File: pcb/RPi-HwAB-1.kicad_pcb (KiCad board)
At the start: 6 copper layers, 65 x 56 mm, 136 parts, among them J1 GPIO, J2 Hirose_FH12-16S, J3 TC2030, M1V1 TestPoint, M1V2 TestPoint, U1 CAT24C256, U10 INA230AIRGTT, U11 MCP9804_DFN, U12 TPSM82903, U13 TPSM82903, U14 AP3441SHE-7B, U2 TPSM82903, U3 LM3880, U4 TXS0102YZP, U5 XC7A100T-FGG484, U6 MT41K256M16LY, U7 TCR2EE135, U8 MX25L3233FZN, U9 INA230AIRGTT, Y1 SiT9365AI-2B2-33E200.000000

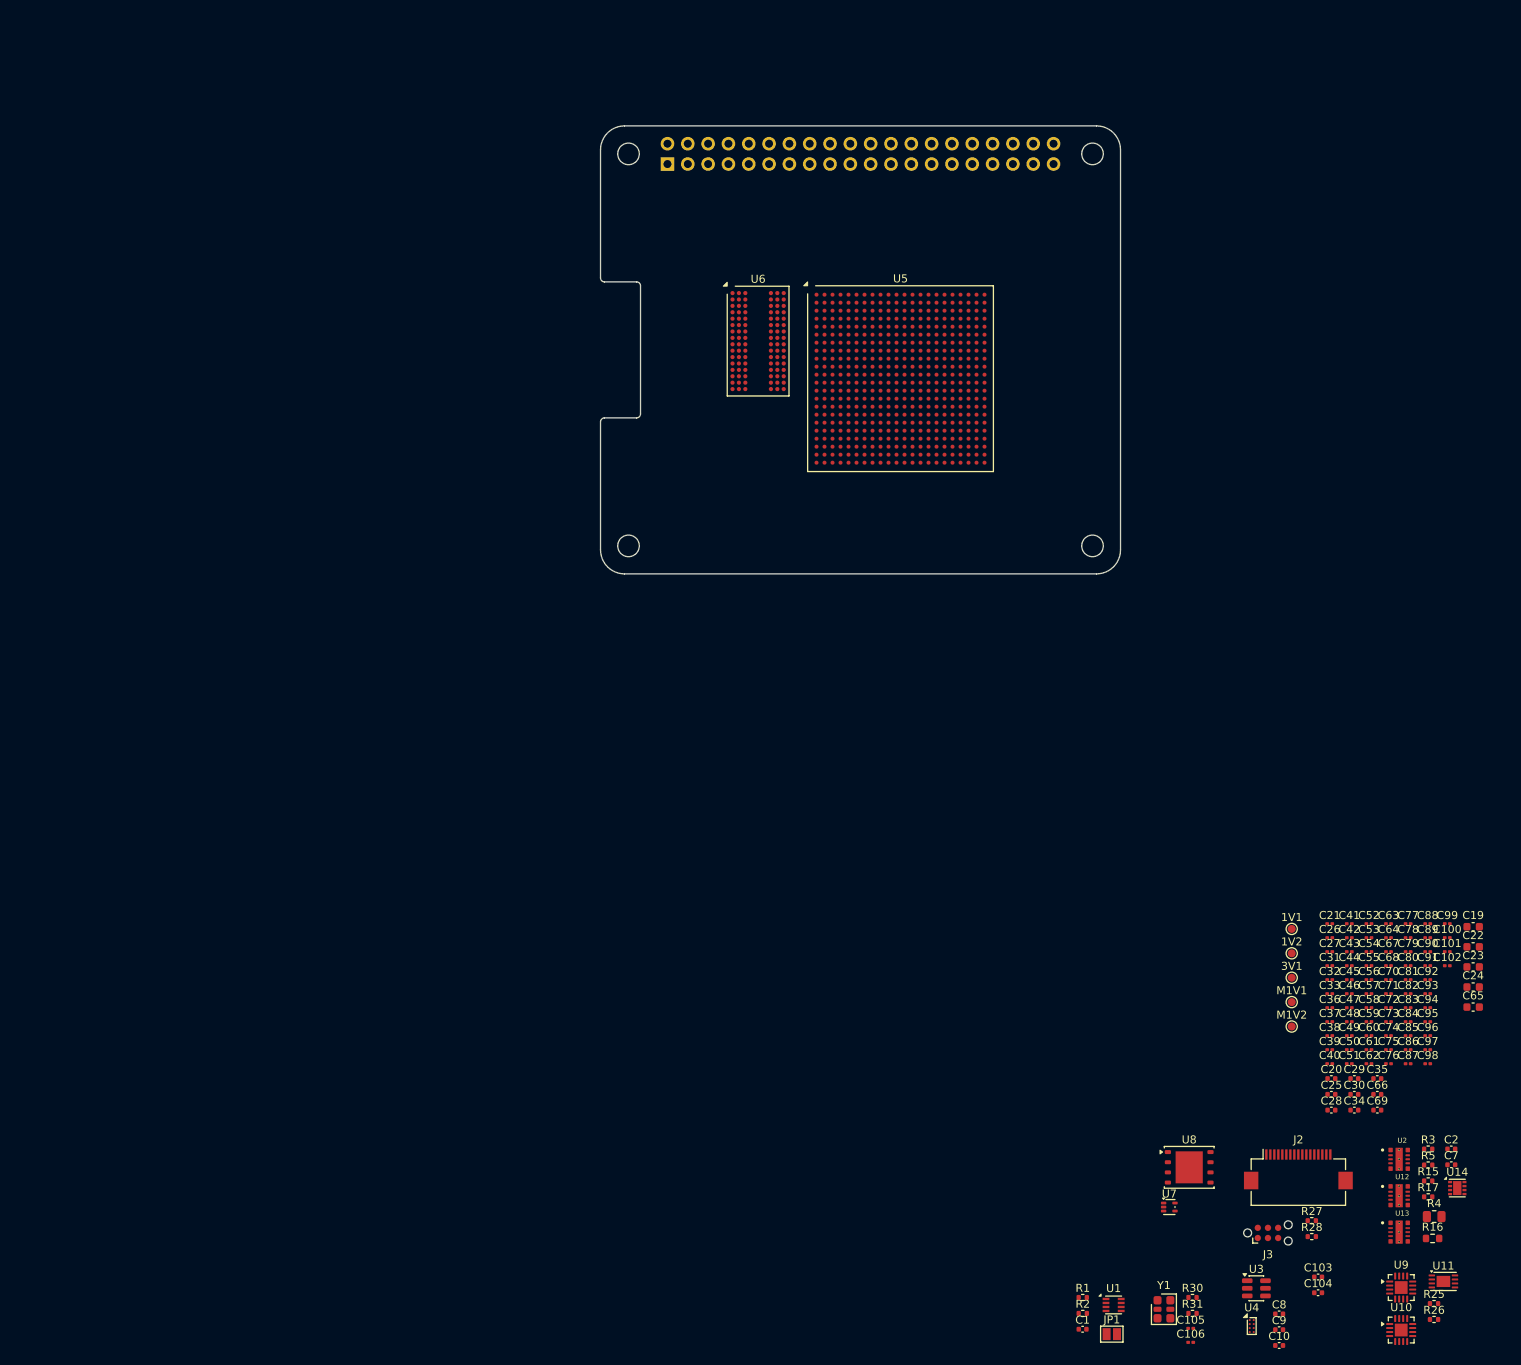
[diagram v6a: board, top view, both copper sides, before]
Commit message: changes to power tree
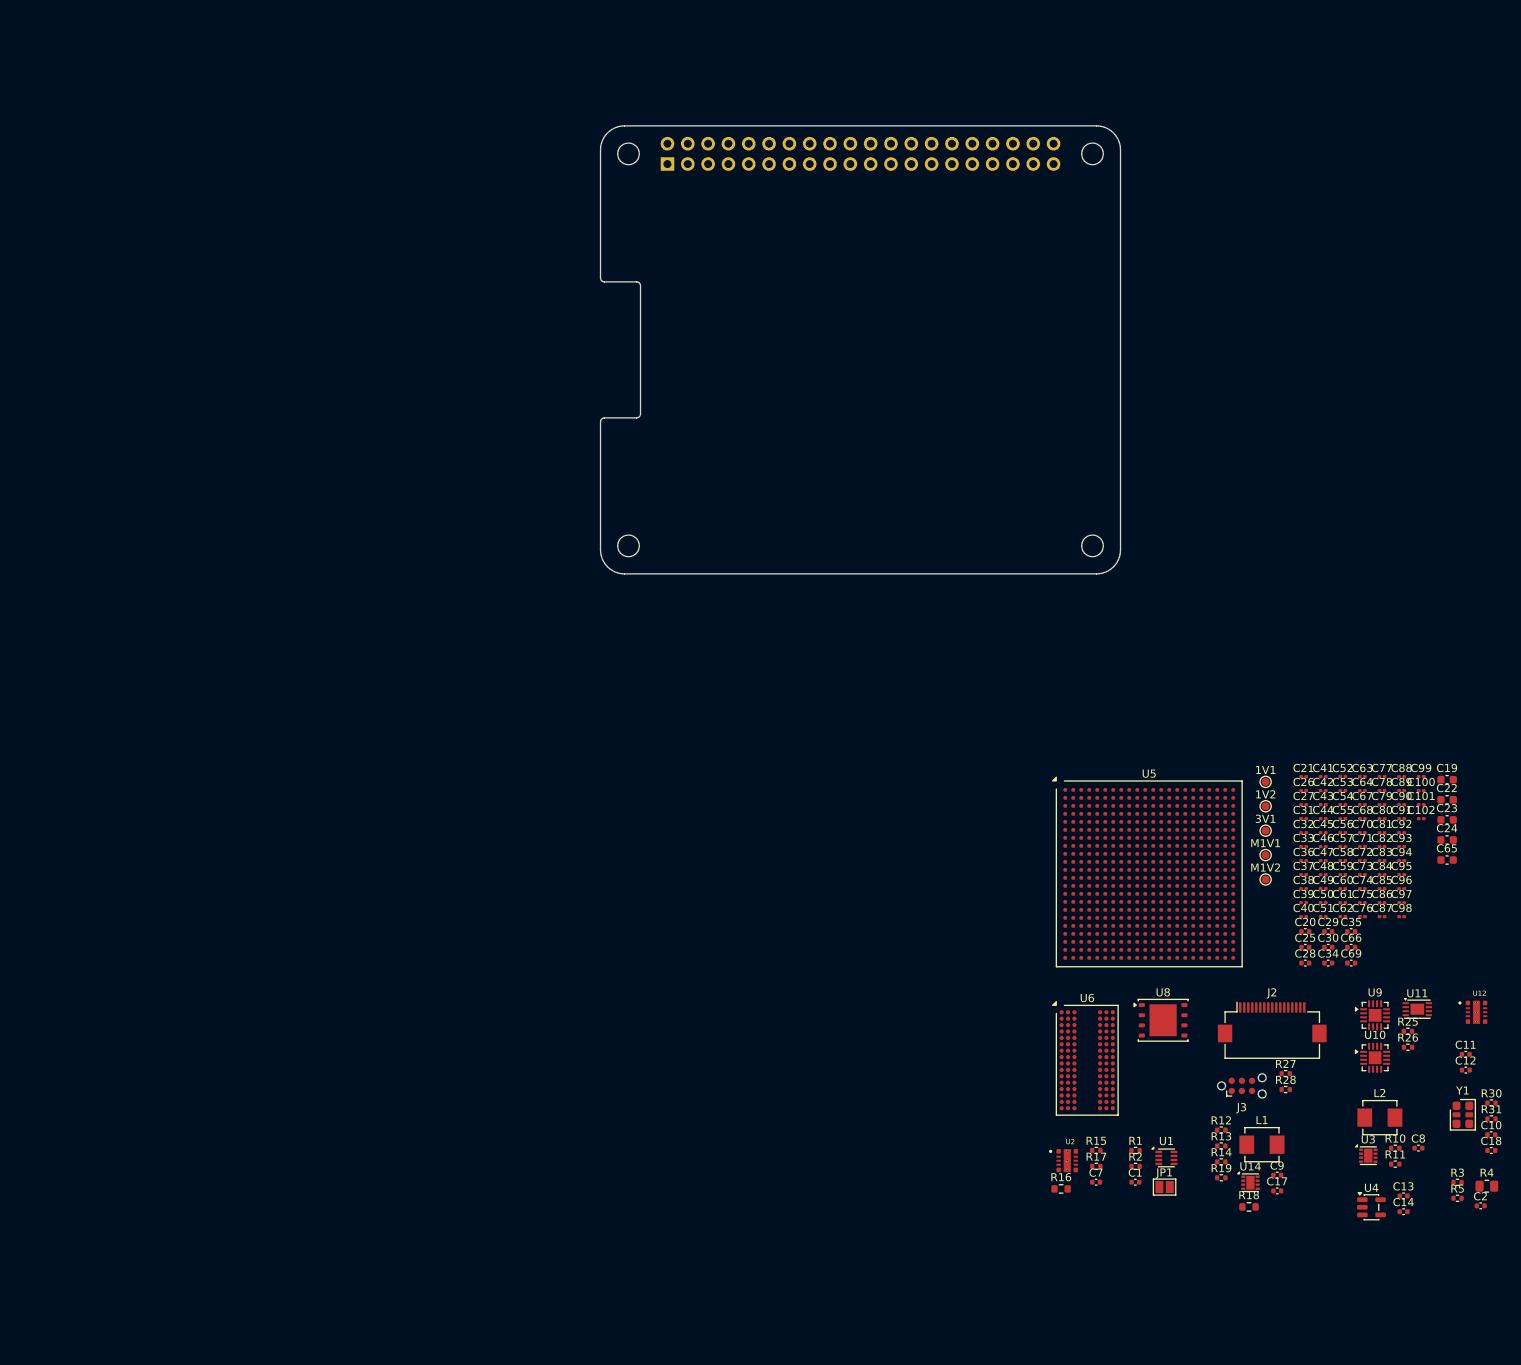
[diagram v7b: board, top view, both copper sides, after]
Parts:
- removed C103, C104: 0.1uF, Capacitor_SMD:C_0402_1005Metric
- removed C105, C106: 0.1uF, Capacitor_SMD:C_0201_0603Metric
- removed U13: TPSM82903, library:TPSM82903SISR
- removed U7: TCR2EE135, Package_TO_SOT_SMD:SOT-553
- added C11: 0.1uF, Capacitor_SMD:C_0402_1005Metric, F.Cu at (208.2, 160.1)
- added C12: 0.1uF, Capacitor_SMD:C_0402_1005Metric, F.Cu at (208.2, 162.0)
- added C13: 1uF, Capacitor_SMD:C_0402_1005Metric, F.Cu at (200.4, 177.8)
- added C14: 1uF, Capacitor_SMD:C_0402_1005Metric, F.Cu at (200.4, 179.7)
- added C17: 0.1uF, Capacitor_SMD:C_0402_1005Metric, F.Cu at (184.6, 177.1)
- added C18: 0.1uF, Capacitor_SMD:C_0402_1005Metric, F.Cu at (211.3, 172.1)
- added L1: 2.2uH, Inductor_SMD:L_Vishay_IHLP-1616, F.Cu at (182.7, 171.3)
- added L2: 2.2uH, Inductor_SMD:L_Vishay_IHLP-1616, F.Cu at (197.4, 168.0)
- added R10: ? 1%, Resistor_SMD:R_0402_1005Metric, F.Cu at (199.3, 171.8)
- added R11: ? 1%, Resistor_SMD:R_0402_1005Metric, F.Cu at (199.3, 173.8)
- added R12: ? 1%, Resistor_SMD:R_0402_1005Metric, F.Cu at (177.6, 169.5)
- added R13: ? 1%, Resistor_SMD:R_0402_1005Metric, F.Cu at (177.6, 171.5)
- added R14: 100, Resistor_SMD:R_0402_1005Metric, F.Cu at (177.6, 173.5)
- added R18: 0.005, Resistor_SMD:R_0603_1608Metric, F.Cu at (181.1, 179.1)
- added R19: 100, Resistor_SMD:R_0402_1005Metric, F.Cu at (177.6, 175.5)
- C8, C9: value 0.1uF -> 4.7nF
- U3: value LM3880 -> AP3441SHE-7B; footprint Package_TO_SOT_SMD:SOT-23-6 -> Package_DFN_QFN:DFN-8-1EP_2x2mm_P0.5mm_EP1.05x1.75mm
- U4: value TXS0102YZP -> TLV74312PDBVR; footprint Package_BGA:Texas_DSBGA-8_0.9x1.9mm_Layout2x4_P0.5mm -> Package_TO_SOT_SMD:SOT-23-5
- moved U6 98.9 mm to (160.8, 160.8)
- moved U5 69.3 mm to (168.6, 137.5)
- moved R16 46.9 mm to (157.6, 176.9)
- moved R30 44.6 mm to (211.4, 166.1)
- moved R31 44.6 mm to (211.4, 168.1)
- moved Y1 44.6 mm to (207.8, 167.6)
- moved C7 44.5 mm to (161.9, 176.0)
- moved R15 41.7 mm to (162.0, 172.1)
- moved R17 41.7 mm to (162.0, 174.1)
- moved U2 41.5 mm to (158.3, 173.3)
- moved C10 37.4 mm to (211.3, 170.1)
- moved U10 34.2 mm to (196.8, 160.5)
- moved U11 34.2 mm to (202.1, 154.4)
- moved U9 34.2 mm to (196.8, 155.2)
- moved R25 34.2 mm to (200.9, 157.2)
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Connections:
- net Net-(C6-Pad1) renamed /Main Power/1V35/1V35_DDR
- net Net-(R16-Pad1) renamed /Main Power/1V0_FD
- net Net-(U12-FB/VSET) renamed /Main Power/1V35/1V35_FB
- net Net-(U2-FB/VSET) renamed /Main Power/1V0/1V0_FB
- C10 pad 1: /Main Power/Sequencing/5V0 -> Net-(U5E-IO_L12N_T1_MRCC_34)
- C10 pad 2: GND -> Net-(Y1-OUT-)
- C2 pad 1: /Main Power/5V0_SENS_P -> /Main Power/5V0_SENS_N
- C2 pad 2: /Main Power/5V0_SENS_N -> /Main Power/5V0_SENS_P
- C22 pad 1: /FPGA/1V0_FD -> /FPGA/1V0_MGT
- C30 pad 1: /FPGA/1V0_FD -> /FPGA/1V0_MGT
- C33 pad 1: /FPGA/1V0_FD -> /FPGA/1V0_MGT
- C38 pad 1: /FPGA/1V0_FD -> /FPGA/1V0_MGT
- C43 pad 1: /FPGA/1V0_FD -> /FPGA/1V0_MGT
- C48 pad 1: /FPGA/1V0_FD -> /FPGA/1V0_MGT
- C8 pad 1: /Main Power/Sequencing/3V3 -> /Main Power/3V3/3V3_FD
- C8 pad 2: GND -> /Main Power/3V3/3V3_FB
- C9 pad 1: /Main Power/Sequencing/5V0 -> /Main Power/1V8_FD
- C9 pad 2: GND -> /Main Power/1V8/1V8_FB
- M1V1 pad 1: /FPGA/1V0_FD -> /FPGA/1V0_MGT
- R15 pad 2: /Main Power/1V0_P -> /Main Power/1V0/1V0_P
- R16 pad 2: /Main Power/1V0_P -> /Main Power/1V0/1V0_P
- R3 pad 1: /Main Power/5V0_SENS_P -> /Main Power/5V0_SENS_N
- R4 pad 2: Net-(R4-Pad2) -> /Main Power/5V0_N
- R5 pad 1: /Main Power/5V0_SENS_N -> /Main Power/5V0_SENS_P
- R5 pad 2: Net-(R4-Pad2) -> /Main Power/5V0_N
- U12 pad 1: Net-(U12-MODE) -> /Main Power/5V0_N
- U12 pad 2: Net-(U12-MODE) -> /Main Power/5V0_N
- U12 pad 3: Net-(U12-EN) -> /Main Power/1V8/1V8_PG
- U12 pad 4: Net-(U12-MODE) -> /Main Power/5V0_N
- U12 pad 6: Net-(U12-PG) -> /Main Power/1V35/1V35_PG
- U14 pad 1: unconnected-(U14-FB-Pad1) -> /Main Power/1V8/1V8_FB
- U14 pad 2: unconnected-(U14-PG-Pad2) -> /Main Power/1V8/1V8_PG
- U14 pad 3: unconnected-(U14-VIN-Pad3) -> /Main Power/5V0_N
- U14 pad 4: unconnected-(U14-PGND-Pad4) -> GND
- U14 pad 6: unconnected-(U14-LX-Pad6) -> /Main Power/1V8/1V8_LX
- U14 pad 7: unconnected-(U14-EN-Pad7) -> /Main Power/1V0/1V0_PG
- U14 pad 8: unconnected-(U14-SGND-Pad8) -> GND
- U14 pad 9: unconnected-(U14-PAD-Pad9) -> GND
- U2 pad 1: Net-(U2-MODE) -> /Main Power/5V0_N
- U2 pad 10: Net-(C4-Pad1) -> /Main Power/1V0/1V0_P
- U2 pad 2: Net-(U2-MODE) -> /Main Power/5V0_N
- U2 pad 4: Net-(U2-MODE) -> /Main Power/5V0_N
- U2 pad 6: Net-(U12-EN) -> /Main Power/1V0/1V0_PG
- U2 pad 9: Net-(C4-Pad1) -> /Main Power/1V0/1V0_P
- U3 pad 1: /Main Power/Sequencing/5V0 -> /Main Power/3V3/3V3_FB
- U3 pad 2: GND -> /Main Power/3V3/3V3_PG
- U3 pad 3: /Main Power/Sequencing/EN1 -> /Main Power/5V0_N
- U3 pad 4: /Main Power/Sequencing/EN4 -> GND
- U3 pad 5: /Main Power/Sequencing/EN3 -> unconnected-(U3-NC-Pad5)
- U3 pad 6: /Main Power/Sequencing/EN2 -> /Main Power/3V3/3V3_LX
- U5 pad F8: Net-(U5G-MGTRREF_216) -> unconnected-(U5G-MGTRREF_216-PadF8)

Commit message: bom
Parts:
- removed 3V1, M1V1, M1V2: TestPoint, TestPoint:TestPoint_Pad_D1.0mm
- removed C11, C12: 0.1uF, Capacitor_SMD:C_0402_1005Metric
- removed C9: 4.7nF, Capacitor_SMD:C_0402_1005Metric
- removed R14, R15: 100, Resistor_SMD:R_0402_1005Metric
- removed R25, R31: 4.7K, Resistor_SMD:R_0402_1005Metric
- removed U8: MX25L3233FZN, Package_SON:WSON-8-1EP_6x5mm_P1.27mm_EP3.4x4mm
- added 1V3: TestPoint, TestPoint:TestPoint_Pad_D1.0mm, F.Cu at (163.1, 121.5)
- added 1V4: TestPoint, TestPoint:TestPoint_Pad_D1.0mm, F.Cu at (146.1, 166.2)
- added 3V3_FD1: TestPoint, TestPoint:TestPoint_Pad_D1.0mm, F.Cu at (158.3, 175.8)
- added C103: 47uF, Capacitor_SMD:C_0603_1608Metric, F.Cu at (106.4, 157.3)
- added C104: 10uF, Capacitor_SMD:C_0402_1005Metric, F.Cu at (121.3, 154.3)
- added C105: 0.1uF, Capacitor_SMD:C_0402_1005Metric, F.Cu at (131.8, 144.4)
- added C106: 0.1uF, Capacitor_SMD:C_0402_1005Metric, F.Cu at (131.8, 146.4)
- added C107: 0.1uF, Capacitor_SMD:C_0402_1005Metric, F.Cu at (131.8, 148.4)
- added C108: 0.1uF, Capacitor_SMD:C_0402_1005Metric, F.Cu at (131.8, 150.3)
- added C16: 4.7nF, Capacitor_SMD:C_0402_1005Metric, F.Cu at (158.5, 169.6)
- added C3: 10uF, library:C_0402_1005Metric, F.Cu at (159.1, 159.6)
- added C4: 4.7nF, Capacitor_SMD:C_0402_1005Metric, F.Cu at (159.1, 161.6)
- added C5: 22uF, library:C_0402_1005Metric, F.Cu at (159.1, 163.5)
- added C6: 0.1uF, Capacitor_SMD:C_0402_1005Metric, F.Cu at (159.1, 165.5)
- added R20: 10, Resistor_SMD:R_0402_1005Metric, F.Cu at (139.1, 162.3)
- added R21: 113K 1%, Resistor_SMD:R_0402_1005Metric, F.Cu at (155.4, 175.2)
- added R22: 24.9K 1%, Resistor_SMD:R_0402_1005Metric, F.Cu at (155.4, 177.2)
- added R23: 4.7K, Resistor_SMD:R_0402_1005Metric, F.Cu at (147.7, 149.4)
- added R24: 4.7K, Resistor_SMD:R_0402_1005Metric, F.Cu at (147.7, 151.4)
- added R29: 100K, library:R_0402_1005Metric, F.Cu at (113.9, 170.5)
- added R6: 100K, library:R_0402_1005Metric, F.Cu at (126.2, 166.4)
- added R7: 100K, library:R_0402_1005Metric, F.Cu at (126.2, 168.3)
- added R8: 100K, library:R_0402_1005Metric, F.Cu at (126.2, 170.3)
- added R9: 10K 1%, library:R_0402_1005Metric, F.Cu at (156.2, 159.6)
- added U13: INA230AIRGTT, Package_DFN_QFN:VQFN-16-1EP_3x3mm_P0.5mm_EP1.6x1.6mm, F.Cu at (127.8, 156.7)
- added U7: XC7A100T-FGG484, library:Xilinx_FGG484, F.Cu at (117.4, 128.4)
- C10: value 0.1uF -> 4.7nF
- C100, C101, C102, C21, C26, C27, C31, C32, C33, C36, C37, C38, C39, C40, C41, C42, C43, C44, C45, C46, C47, C48, C49, C50, C51, C52, C53, C54, C55, C56, C57, C58, C59, C60, C61, C62, C63, C64, C67, C68, C74, C75, C78, C79, C80, C82, C83, C84, C85, C86, C87, C88, C89, C90, C92, C93, C94, C96, C97, C98, C99: footprint Capacitor_SMD:C_0201_0603Metric -> Capacitor_SMD:C_0402_1005Metric
- C13: value 1uF -> 4.7nF
- C14: value 1uF -> 0.1uF
- C19, C23, C24, C65: value 47uF -> 0.1uF; footprint Capacitor_SMD:C_0603_1608Metric -> Capacitor_SMD:C_0402_1005Metric
- C22: value 10uF -> 0.1uF; footprint Capacitor_SMD:C_0603_1608Metric -> Capacitor_SMD:C_0402_1005Metric
- C25, C28, C29: value 10uF -> 0.1uF
- C69: value 10uF -> 47uF; footprint Capacitor_SMD:C_0402_1005Metric -> Capacitor_SMD:C_0603_1608Metric
- C7: value 0.1uF -> 1uF
- C70, C71, C76, C81, C95: value 0.1uF -> 10uF; footprint Capacitor_SMD:C_0201_0603Metric -> Capacitor_SMD:C_0402_1005Metric
- C72, C73, C77, C91: value 0.1uF -> 47uF; footprint Capacitor_SMD:C_0201_0603Metric -> Capacitor_SMD:C_0603_1608Metric
- C8: value 4.7nF -> 1uF
- R10: value ? 1% -> 15K 1%; footprint Resistor_SMD:R_0402_1005Metric -> library:R_0402_1005Metric
- R11, R13: value ? 1% -> 10
- R12: value ? 1% -> 0.005; footprint Resistor_SMD:R_0402_1005Metric -> Resistor_SMD:R_1206_3216Metric
- R16: value 0.005 -> 30K 1%; footprint Resistor_SMD:R_0603_1608Metric -> Resistor_SMD:R_0402_1005Metric
- R17: value 100 -> 15K 1%
- R18: value 0.005 -> 10; footprint Resistor_SMD:R_0603_1608Metric -> Resistor_SMD:R_0402_1005Metric
- R19: value 100 -> 0.005; footprint Resistor_SMD:R_0402_1005Metric -> Resistor_SMD:R_0603_1608Metric
- R26: value 4.7K -> 240 1%
- R27: value 100K -> 4.7K
- R28: value 2.2K -> 4.7K
- R3, R5: value 100 -> 10
- R30: value 4.7K -> 2.2K
- R4: value 0.003 -> 0.003 1%; footprint Resistor_SMD:R_0805_2012Metric -> Resistor_SMD:R_1206_3216Metric
- U10: value INA230AIRGTT -> MX25L12835F; footprint Package_DFN_QFN:VQFN-16-1EP_3x3mm_P0.5mm_EP1.6x1.6mm -> Package_SON:WSON-8-1EP_6x5mm_P1.27mm_EP3.4x4mm
- U11: value MCP9804_DFN -> INA230AIRGTT; footprint Package_DFN_QFN:DFN-8-1EP_3x2mm_P0.5mm_EP1.7x1.4mm -> Package_DFN_QFN:VQFN-16-1EP_3x3mm_P0.5mm_EP1.6x1.6mm
- U12: value TPSM82903 -> INA230AIRGTT; footprint library:TPSM82903SISR -> Package_DFN_QFN:VQFN-16-1EP_3x3mm_P0.5mm_EP1.6x1.6mm
- U14: value AP3441SHE-7B -> MCP9804_DFN; footprint Package_DFN_QFN:DFN-8-1EP_2x2mm_P0.5mm_EP1.05x1.75mm -> Package_DFN_QFN:DFN-8-1EP_3x2mm_P0.5mm_EP1.7x1.4mm
- U3: value AP3441SHE-7B -> TLV74312PDBVR; footprint Package_DFN_QFN:DFN-8-1EP_2x2mm_P0.5mm_EP1.05x1.75mm -> Package_TO_SOT_SMD:SOT-23-5
- U4: value TLV74312PDBVR -> TPSM82903; footprint Package_TO_SOT_SMD:SOT-23-5 -> library:TPSM82903SISR
- U5: value XC7A100T-FGG484 -> AP3441SHE-7B; footprint library:Xilinx_FGG484 -> Package_DFN_QFN:DFN-8-1EP_2x2mm_P0.5mm_EP1.05x1.75mm
- U6: value MT41K256M16LY -> AP3441SHE-7B; footprint Package_BGA:Micron_FBGA-96_7.5x13.5mm_Layout9x16_P0.8mm -> Package_DFN_QFN:DFN-8-1EP_2x2mm_P0.5mm_EP1.05x1.75mm
- U9: value INA230AIRGTT -> MT41K256M16LY; footprint Package_DFN_QFN:VQFN-16-1EP_3x3mm_P0.5mm_EP1.6x1.6mm -> Package_BGA:Micron_FBGA-96_7.5x13.5mm_Layout9x16_P0.8mm
- moved R30 97.7 mm to (113.9, 172.4)
- moved C91 96.8 mm to (106.4, 154.8)
- moved C18 95.9 mm to (131.8, 118.4)
- moved C77 95.2 mm to (106.4, 152.2)
- moved C78 92.0 mm to (109.8, 154.3)
- moved C73 89.7 mm to (106.4, 149.7)
- moved C72 89.6 mm to (106.4, 147.2)
- moved C90 88.3 mm to (115.5, 154.3)
- moved C89 88.3 mm to (115.5, 152.3)
- moved C88 88.2 mm to (115.5, 150.3)
- moved C69 87.6 mm to (106.4, 144.7)
- moved C84 86.6 mm to (112.7, 154.3)
- moved C83 86.6 mm to (112.7, 152.3)
- moved C82 86.5 mm to (112.7, 150.3)
- moved C81 86.5 mm to (112.7, 148.4)
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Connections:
- net /Connectors/SPI0.CS1 renamed /Connectors/QSPI0.CS1n
- 1V1 pad 1: /FPGA/1V0_FD -> /Main Power/1V0_FD
- 1V2 pad 1: /FPGA/1V8_FD -> /Main Power/1V2_MGT
- C10 pad 1: Net-(U5E-IO_L12N_T1_MRCC_34) -> Net-(U4-SS/TR)
- C10 pad 2: Net-(Y1-OUT-) -> GND
- C100 pad 2: GND -> /Main Power/1V0_FD
- C101 pad 2: GND -> /Main Power/1V0_FD
- C102 pad 2: GND -> /Main Power/1V0_FD
- C13 pad 1: /Main Power/1V8_FD -> /Main Power/1V8/1V8_P
- C13 pad 2: GND -> /Main Power/1V8/1V8_FB
- C14 pad 1: /Main Power/1V2_MGT -> /Main Power/1V8_SENS_N
- C14 pad 2: GND -> /Main Power/1V8_SENS_P
- C17 pad 1: /Main Power/1V8_SENS_N -> GND
- C17 pad 2: /Main Power/1V8_SENS_P -> /Main Power/3V3_FD
- C18 pad 1: Net-(U5E-IO_L12P_T1_MRCC_34) -> GND
- C18 pad 2: Net-(Y1-OUT+) -> /Main Power/3V3_FD
- C19 pad 1: /FPGA/1V0_FD -> GND
- C19 pad 2: GND -> /Main Power/3V3_FD
- C20 pad 1: /FPGA/1V0_FD -> GND
- C20 pad 2: GND -> /Main Power/3V3_FD
- C21 pad 1: /FPGA/1V0_FD -> GND
- C21 pad 2: GND -> /Main Power/3V3_FD
- C22 pad 1: /FPGA/1V0_MGT -> GND
- C22 pad 2: GND -> /Main Power/3V3_FD
- C23 pad 1: /FPGA/1V2_MGT -> GND
- C23 pad 2: GND -> /Main Power/3V3_FD
- C24 pad 1: /FPGA/1V8_FD -> GND
- C24 pad 2: GND -> /Main Power/3V3_FD
- C25 pad 1: /FPGA/1V0_FD -> GND
- C25 pad 2: GND -> /Main Power/3V3_FD
- C26 pad 1: /FPGA/1V0_FD -> GND
- C26 pad 2: GND -> /Main Power/3V3_FD
- C27 pad 1: /FPGA/1V0_FD -> GND
- C27 pad 2: GND -> /Main Power/3V3_FD
- C28 pad 1: /FPGA/1V2_MGT -> GND
- C28 pad 2: GND -> /Main Power/3V3_FD
- C29 pad 1: /FPGA/1V8_FD -> GND
- C29 pad 2: GND -> /Main Power/3V3_FD
- C30 pad 1: /FPGA/1V0_MGT -> GND
- C30 pad 2: GND -> /Main Power/3V3_FD
- C31 pad 1: /FPGA/1V0_FD -> GND
- C31 pad 2: GND -> /Main Power/3V3_FD
- C32 pad 1: /FPGA/1V0_FD -> GND
- C32 pad 2: GND -> /Main Power/3V3_FD
- C33 pad 1: /FPGA/1V0_MGT -> GND
- C33 pad 2: GND -> /Main Power/3V3_FD
- C34 pad 1: /FPGA/1V2_MGT -> GND
- C34 pad 2: GND -> /Main Power/3V3_FD
- C35 pad 1: /FPGA/1V8_FD -> GND
- C35 pad 2: GND -> /Main Power/3V3_FD
- C36 pad 1: /FPGA/1V0_FD -> GND
- C36 pad 2: GND -> /Main Power/3V3_FD
- C37 pad 1: /FPGA/1V0_FD -> GND
- C37 pad 2: GND -> /Main Power/3V3_FD
- C38 pad 1: /FPGA/1V0_MGT -> GND
- C38 pad 2: GND -> /Main Power/3V3_FD
- C39 pad 1: /FPGA/1V2_MGT -> GND
- C39 pad 2: GND -> /Main Power/3V3_FD
- C40 pad 1: /FPGA/1V8_FD -> GND
- C40 pad 2: GND -> /Main Power/3V3_FD
- C41 pad 1: /FPGA/1V0_FD -> GND
- C41 pad 2: GND -> /Main Power/3V3_FD
- C42 pad 1: /FPGA/1V0_FD -> Net-(U7E-IO_L12N_T1_MRCC_34)
- C42 pad 2: GND -> Net-(Y1-OUT-)
- C43 pad 1: /FPGA/1V0_MGT -> Net-(U7E-IO_L12P_T1_MRCC_34)
- C43 pad 2: GND -> Net-(Y1-OUT+)
- C44 pad 1: /FPGA/1V2_MGT -> GND
- C44 pad 2: GND -> /Main Power/1V35_DDR
- C45 pad 1: /FPGA/1V8_FD -> GND
- C45 pad 2: GND -> /Main Power/1V35_DDR
- C46 pad 1: /FPGA/1V0_FD -> GND
- C46 pad 2: GND -> /Main Power/1V35_DDR
- C47 pad 1: /FPGA/1V0_FD -> GND
- C47 pad 2: GND -> /Main Power/1V35_DDR
- C48 pad 1: /FPGA/1V0_MGT -> GND
- C48 pad 2: GND -> /Main Power/1V35_DDR
- C49 pad 1: /FPGA/1V2_MGT -> GND
- C49 pad 2: GND -> /Main Power/1V35_DDR
- C50 pad 1: /FPGA/1V8_FD -> GND
- C50 pad 2: GND -> /Main Power/1V35_DDR
- C51 pad 1: /FPGA/1V0_FD -> GND
- C51 pad 2: GND -> /Main Power/1V35_DDR
- C52 pad 1: /FPGA/1V0_FD -> GND
- C52 pad 2: GND -> /Main Power/1V35_DDR
- C53 pad 1: /FPGA/1V2_MGT -> GND
- C53 pad 2: GND -> /Main Power/1V35_DDR
- C54 pad 1: /FPGA/1V8_FD -> GND
- C54 pad 2: GND -> /Main Power/1V35_DDR
- C55 pad 1: /FPGA/1V0_FD -> GND
- C55 pad 2: GND -> /Main Power/1V35_DDR
- C56 pad 1: /FPGA/1V0_FD -> GND
- C56 pad 2: GND -> /Main Power/1V0_MGT
- C57 pad 1: /FPGA/1V2_MGT -> GND
- C57 pad 2: GND -> /Main Power/1V2_MGT
- C58 pad 1: /FPGA/1V8_FD -> GND
- C58 pad 2: GND -> /Main Power/1V0_MGT
- C59 pad 1: /FPGA/1V0_FD -> GND
- C59 pad 2: GND -> /Main Power/1V2_MGT
- C60 pad 1: /FPGA/1V0_FD -> GND
- C60 pad 2: GND -> /Main Power/1V0_MGT
- C61 pad 1: /FPGA/1V0_FD -> GND
- C61 pad 2: GND -> /Main Power/1V2_MGT
- C62 pad 1: /FPGA/1V0_FD -> GND
- C62 pad 2: GND -> /Main Power/1V0_MGT
- C63 pad 1: /FPGA/1V0_FD -> GND
- C63 pad 2: GND -> /Main Power/1V2_MGT
- C64 pad 1: /FPGA/1V0_FD -> GND
- C64 pad 2: GND -> /Main Power/1V0_MGT
- C65 pad 2: Net-(C65-Pad2) -> /Main Power/1V2_MGT
- C66 pad 2: GND -> /Main Power/1V2_MGT
- C67 pad 1: GND -> /FPGA/FPGA 4/F2P_N
- C67 pad 2: GND -> /Connectors/PCIE.F2P_P
- C68 pad 1: GND -> /FPGA/FPGA 4/F2P_P
- C68 pad 2: GND -> /Connectors/PCIE.F2P_N
- C69 pad 1: GND -> /Main Power/1V0_MGT
- C69 pad 2: Net-(C65-Pad2) -> GND
- C7 pad 1: /Main Power/1V0_SENS_P -> /Main Power/1V8_FD
- C7 pad 2: /Main Power/1V0_SENS_N -> GND
- C70 pad 1: GND -> /Main Power/1V0_MGT
- C71 pad 1: GND -> /Main Power/1V0_FD
- C72 pad 1: GND -> /Main Power/1V0_FD
- C73 pad 1: GND -> /Main Power/1V8_FD
- C74 pad 2: GND -> /Main Power/1V0_FD
- C75 pad 2: GND -> /Main Power/1V0_FD
- C76 pad 1: GND -> /Main Power/1V8_FD
- C77 pad 1: GND -> /Main Power/1V2_MGT
- C78 pad 2: GND -> /Main Power/1V0_FD
- C79 pad 2: GND -> /Main Power/1V0_FD
- C8 pad 1: /Main Power/3V3/3V3_FD -> /Main Power/1V2_MGT
- C8 pad 2: /Main Power/3V3/3V3_FB -> GND
- C80 pad 2: GND -> /Main Power/1V8_FD
- C81 pad 1: GND -> /Main Power/1V2_MGT
- C82 pad 2: GND -> /Main Power/1V0_FD
- C83 pad 2: GND -> /Main Power/1V0_FD
- C84 pad 2: GND -> /Main Power/1V8_FD
- C85 pad 2: GND -> /Main Power/1V0_FD
- C86 pad 2: GND -> /Main Power/1V0_FD
- C87 pad 2: GND -> /Main Power/1V8_FD
- C88 pad 2: GND -> /Main Power/1V0_FD
- C89 pad 2: GND -> /Main Power/1V0_FD
- C90 pad 2: GND -> /Main Power/1V8_FD
- C91 pad 1: GND -> /Main Power/3V3_FD
- C92 pad 2: GND -> /Main Power/1V0_FD
- C93 pad 2: GND -> /Main Power/1V0_FD
- C94 pad 2: GND -> /Main Power/1V8_FD
- C95 pad 1: GND -> /Main Power/3V3_FD
- C96 pad 2: GND -> /Main Power/1V0_FD
- C97 pad 2: GND -> /Main Power/1V0_FD
- C98 pad 2: GND -> /Main Power/1V8_FD
- C99 pad 2: GND -> /Main Power/1V0_FD
- J1 pad 18: /Connectors/PGOOD -> /Main Power/3V3/3V3_PG
- J1 pad 19: /Connectors/SPI0.MOSI -> /Connectors/QSPI0.SIO0
- J1 pad 21: /Connectors/SPI0.MISO -> /Connectors/QSPI0.SIO1
- J1 pad 23: /Connectors/SPI0.SCK -> /Connectors/QSPI0.SCLK
- J1 pad 24: /Connectors/SPI0.CS0 -> /Connectors/QSPI0.CS0n
- J1 pad 33: unconnected-(J1-Pin_33-Pad33) -> /Connectors/TCK
- J1 pad 35: unconnected-(J1-Pin_35-Pad35) -> /Connectors/TMS
- J1 pad 36: unconnected-(J1-Pin_36-Pad36) -> /Connectors/TDO
- J1 pad 37: unconnected-(J1-Pin_37-Pad37) -> /Connectors/TDI
- J1 pad 38: unconnected-(J1-Pin_38-Pad38) -> /Connectors/PROG_B
- J1 pad 40: unconnected-(J1-Pin_40-Pad40) -> /Connectors/DONE
- L1 pad 2: /Main Power/1V8_FD -> /Main Power/1V8/1V8_P
- L2 pad 2: /Main Power/3V3/3V3_FD -> /Main Power/3V3_FD
- R10 pad 1: /Main Power/3V3/3V3_FD -> /Main Power/1V0/1V0_FB
- R10 pad 2: /Main Power/3V3/3V3_FB -> GND
- R11 pad 1: /Main Power/3V3/3V3_FB -> /Main Power/1V0_SENS_N
- R11 pad 2: GND -> /Main Power/1V0/1V0_P
- R12 pad 1: /Main Power/1V8_FD -> /Main Power/1V0_FD
- R12 pad 2: /Main Power/1V8/1V8_FB -> /Main Power/1V0/1V0_P
- R13 pad 1: /Main Power/1V8/1V8_FB -> /Main Power/1V0_SENS_P
- R13 pad 2: GND -> /Main Power/1V0_FD
- R16 pad 1: /Main Power/1V0_FD -> /Main Power/1V8/1V8_P
- R16 pad 2: /Main Power/1V0/1V0_P -> /Main Power/1V8/1V8_FB
- R17 pad 1: /Main Power/1V0_SENS_P -> /Main Power/1V8/1V8_FB
- R17 pad 2: /Main Power/1V0_FD -> GND
- R18 pad 1: /Main Power/1V8_FD -> /Main Power/1V8_SENS_P
- R18 pad 2: /Main Power/1V8_FD -> /Main Power/1V8/1V8_P
- R19 pad 1: /Main Power/1V8_SENS_N -> /Main Power/1V8_FD
- R19 pad 2: /Main Power/1V8_FD -> /Main Power/1V8/1V8_P
- R26 pad 1: /Connectors/3V3 -> Net-(U9-ZQ)
- R26 pad 2: /Connectors/I2C1.SCL -> /Main Power/1V35_DDR
- R27 pad 1: /Connectors/PCIE.PWR_EN -> /Connectors/3V3
- R27 pad 2: GND -> /Connectors/I2C1.SDA
- R28 pad 2: /Connectors/PCIE.DET_WAKE -> /Connectors/I2C1.SCL
- R30 pad 1: /FPGA/FPGA 3/1V35_FD -> /Connectors/3V3
- R30 pad 2: Net-(U5E-IO_L12P_T1_MRCC_34) -> /Connectors/PCIE.DET_WAKE
- U10 pad 1: GND -> /Connectors/QSPI0.CS0n
- U10 pad 2: /Connectors/3V3 -> /Connectors/QSPI0.SIO1
- U10 pad 3: unconnected-(U10-ALERT-Pad3) -> /Connectors/QSPI0.SIO2
- U10 pad 4: /Connectors/I2C1.SDA -> GND
- U10 pad 5: /Connectors/I2C1.SCL -> /Connectors/QSPI0.SIO0
- U10 pad 6: GND -> /Connectors/QSPI0.SCLK
- U10 pad 7: GND -> /Connectors/QSPI0.SIO3
- U10 pad 8: /Connectors/3V3 -> /Main Power/3V3_FD
- U10 pad 9: (no net) -> GND
- U11 pad 1: /Connectors/I2C1.SDA -> GND
- U11 pad 2: /Connectors/I2C1.SCL -> GND
- U11 pad 4: GND -> /Connectors/I2C1.SDA
- U11 pad 5: GND -> /Connectors/I2C1.SCL
- U11 pad 9: GND -> (no net)
- U12 pad 1: /Main Power/5V0_N -> GND
- U12 pad 10: /Main Power/1V35/1V35_DDR -> GND
- U12 pad 11: GND -> /Main Power/1V0_SENS_P
- U12 pad 12: (no net) -> /Main Power/1V0_SENS_N
- U12 pad 13: (no net) -> /Main Power/1V0_SENS_P
- U12 pad 14: (no net) -> unconnected-(U12-NC-Pad14)
- U12 pad 2: /Main Power/5V0_N -> /Connectors/3V3
- U12 pad 3: /Main Power/1V8/1V8_PG -> unconnected-(U12-ALERT-Pad3)
- U12 pad 4: /Main Power/5V0_N -> /Connectors/I2C1.SDA
- U12 pad 5: unconnected-(U12-SS/TR-Pad5) -> /Connectors/I2C1.SCL
- U12 pad 6: /Main Power/1V35/1V35_PG -> GND
- U12 pad 7: /Main Power/1V35/1V35_FB -> GND
- U12 pad 8: unconnected-(U12-SW-Pad8) -> /Connectors/3V3
- U12 pad 9: /Main Power/1V35/1V35_DDR -> (no net)
- U14 pad 1: /Main Power/1V8/1V8_FB -> /Connectors/I2C1.SDA
- U14 pad 2: /Main Power/1V8/1V8_PG -> /Connectors/I2C1.SCL
- U14 pad 3: /Main Power/5V0_N -> unconnected-(U14-Alert-Pad3)
- U14 pad 5: unconnected-(U14-NC-Pad5) -> GND
- U14 pad 6: /Main Power/1V8/1V8_LX -> GND
- U14 pad 7: /Main Power/1V0/1V0_PG -> GND
- U14 pad 8: GND -> /Connectors/3V3
- U2 pad 5: unconnected-(U2-SS/TR-Pad5) -> Net-(U2-SS/TR)
- U3 pad 1: /Main Power/3V3/3V3_FB -> /Main Power/1V8_FD
- U3 pad 2: /Main Power/3V3/3V3_PG -> GND
- U3 pad 3: /Main Power/5V0_N -> /Main Power/1V8_FD
- U3 pad 4: GND -> unconnected-(U3-NC-Pad4)
- U3 pad 5: unconnected-(U3-NC-Pad5) -> /Main Power/1V2_MGT
- U4 pad 1: /Main Power/1V8_FD -> /Main Power/5V0_N
- U4 pad 2: GND -> /Main Power/5V0_N
- U4 pad 3: /Main Power/1V8_FD -> /Main Power/1V8/1V8_PG
- U4 pad 4: unconnected-(U4-NC-Pad4) -> /Main Power/5V0_N
- U4 pad 5: /Main Power/1V2_MGT -> Net-(U4-SS/TR)
- Y1 pad 1: /FPGA/FPGA 3/3V3_FD -> /Main Power/3V3_FD
- Y1 pad 6: /FPGA/FPGA 3/3V3_FD -> /Main Power/3V3_FD
